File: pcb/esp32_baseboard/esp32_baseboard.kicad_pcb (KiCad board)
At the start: 2 copper layers, 180 x 120 mm, 84 parts, among them J1 24V_IN, J14 BUP_U, J15 FIBER, U1 STM32G030, U2 MP1584EN, U3 TMC2209, U4 TMC2209, U44 PC817, U45 PC817, U46 PC817, U47 PC817, U5 CH340C, U6 AMS1117-3.3, Y1 12MHz

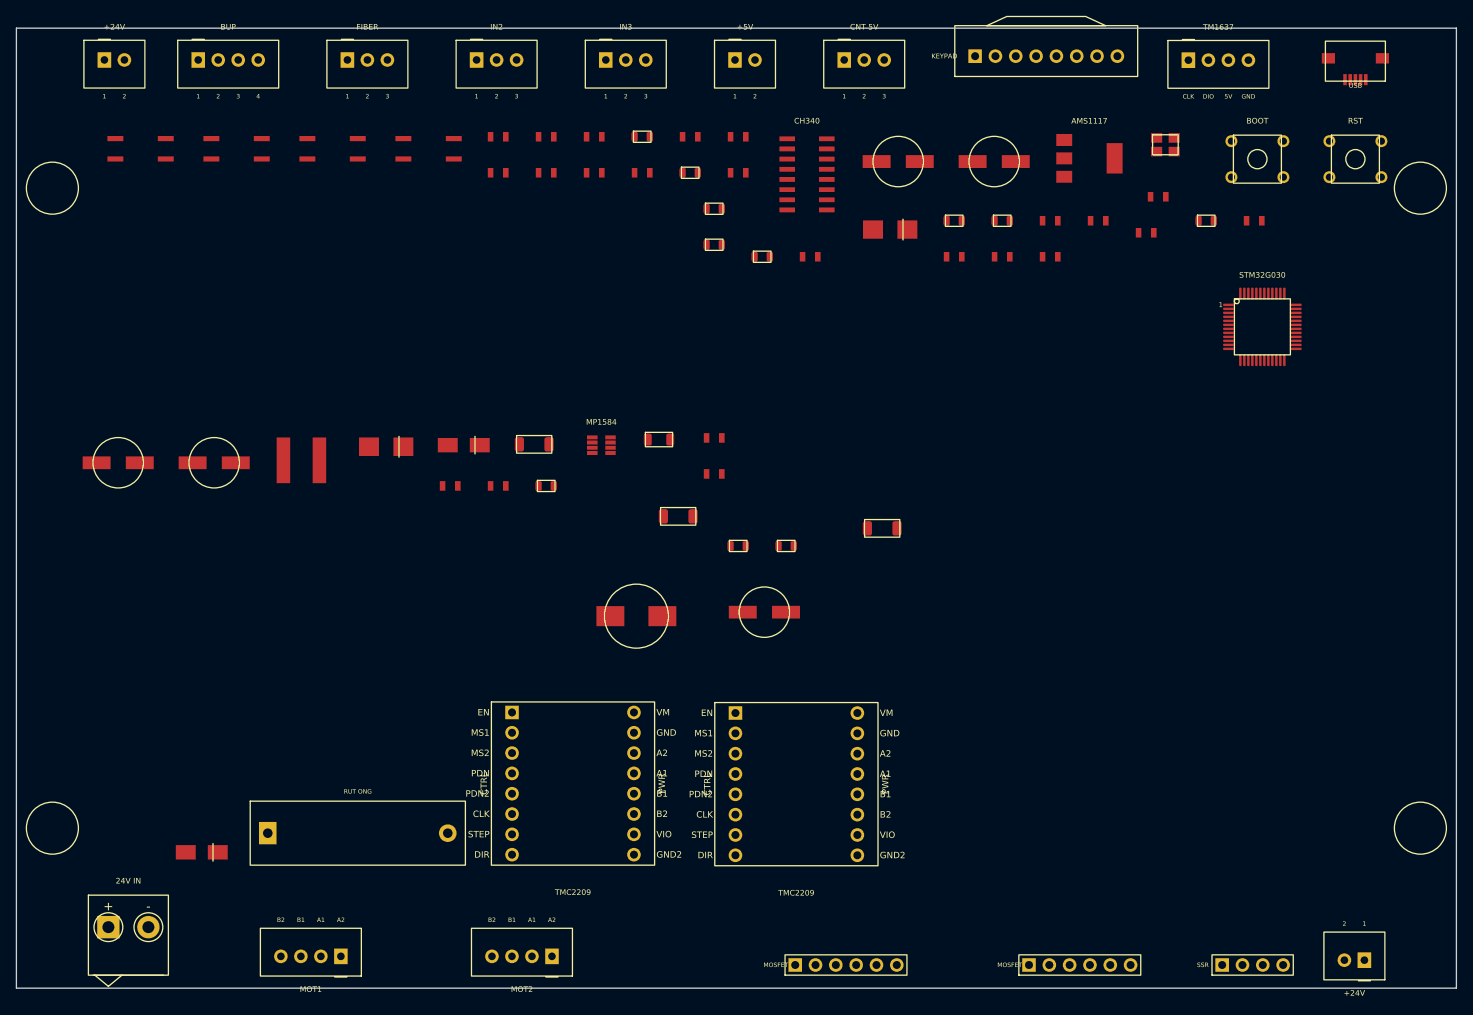
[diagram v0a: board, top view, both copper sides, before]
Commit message: thêm review JLCPCB và cập nhật BOM, bỏ tracking JRE/out.
Co-authored-by: Cursor <cursoragent@cursor.com>
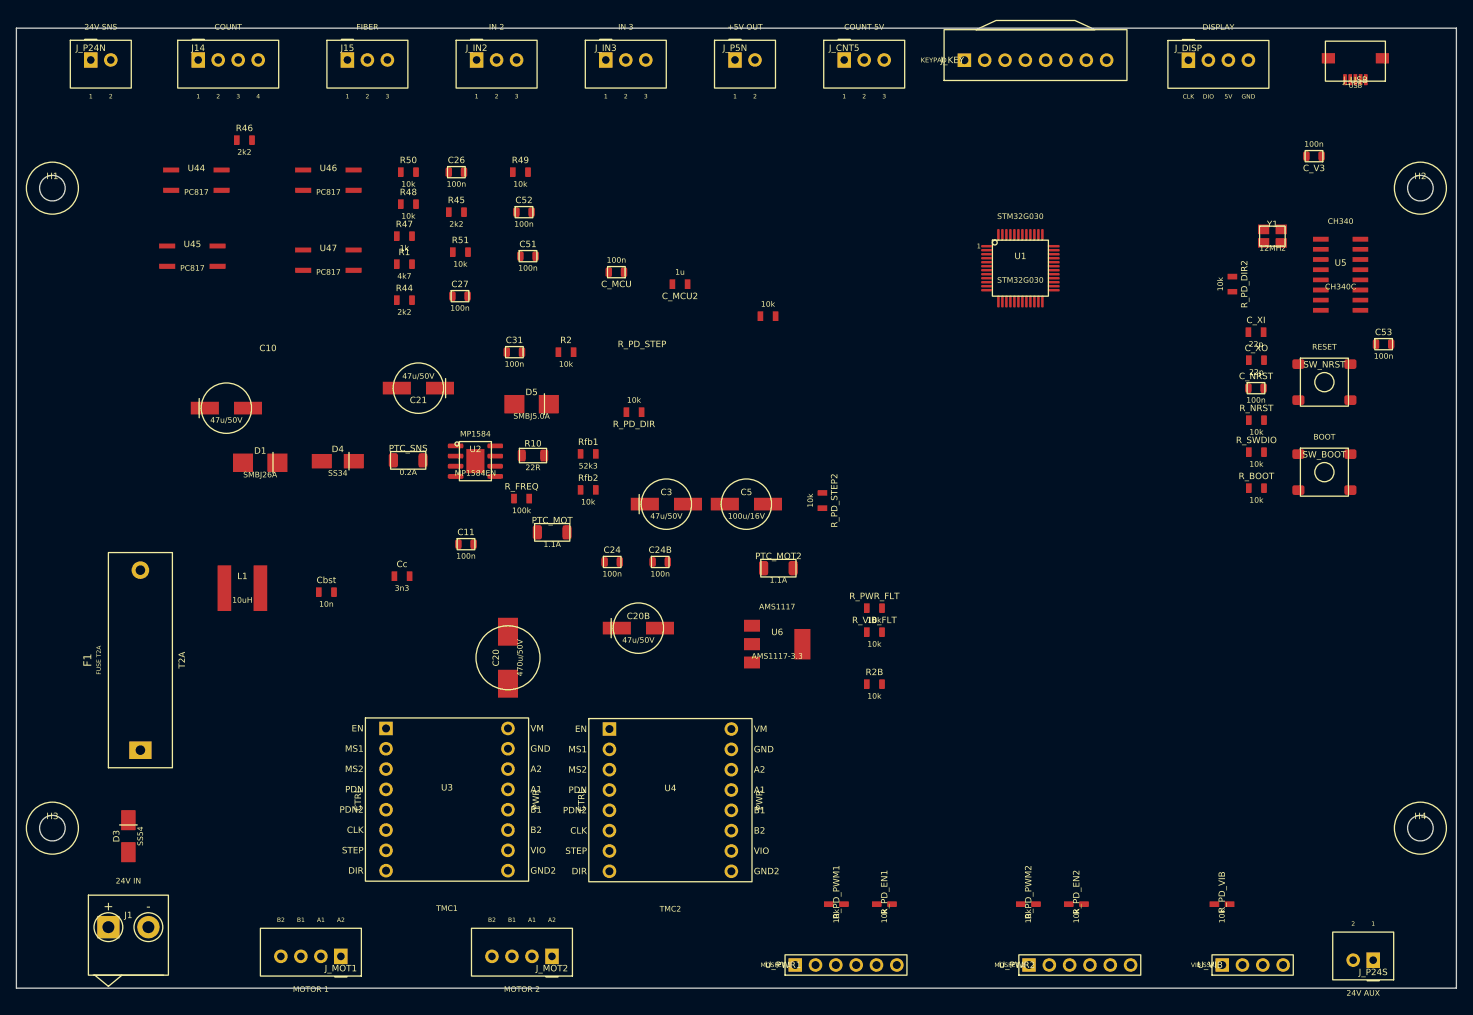
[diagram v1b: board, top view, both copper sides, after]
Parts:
- removed the C20B at (143.5, 123.0)
- added C20B: 47u/50V, ESP32_Carrier:CP_SMD_D6.3x8, F.Cu at (127.8, 125.0)
- added C_V3: 100n, ESP32_Carrier:C_0805_100n, F.Cu at (212.2, 66.0)
- added R_FREQ: 100k, ESP32_Carrier:R_0805_100k, F.Cu at (113.2, 108.8)
- added R_PD_DIR: 10k, ESP32_Carrier:R_0805_10k, F.Cu at (127.2, 98.0)
- added R_PD_DIR2: 10k, ESP32_Carrier:R_0805_10k, F.Cu at (202.0, 82.0)
- added R_PD_EN1: 10k, ESP32_Carrier:R_0805_10k, F.Cu at (158.5, 159.5)
- added R_PD_EN2: 10k, ESP32_Carrier:R_0805_10k, F.Cu at (182.5, 159.5)
- added R_PD_PWM1: 10k, ESP32_Carrier:R_0805_10k, F.Cu at (152.5, 159.5)
- added R_PD_PWM2: 10k, ESP32_Carrier:R_0805_10k, F.Cu at (176.5, 159.5)
- added R_PD_STEP: 10k, ESP32_Carrier:R_0805_10k, F.Cu at (143.9, 86.0)
- added R_PD_STEP2: 10k, ESP32_Carrier:R_0805_10k, F.Cu at (150.8, 109.0)
- added R_PD_VIB: 10k, ESP32_Carrier:R_0805_10k, F.Cu at (200.7, 159.5)
- C10: footprint ESP32_Carrier:CP_SMD_D6.3x5.8 -> ESP32_Carrier:CP_SMD_D6.3x8
- C21: value 220u/50V -> 47u/50V; footprint ESP32_Carrier:CP_SMD_D6.3x5.8 -> ESP32_Carrier:CP_SMD_D6.3x8
- C3: value 47u/10V -> 47u/50V; footprint ESP32_Carrier:CP_SMD_D6.3x5.8 -> ESP32_Carrier:CP_SMD_D6.3x8
- J1: value 24V_IN -> 24V IN
- J14: value BUP_U -> COUNT
- J_CNT5: value CNT5V -> COUNT 5V
- J_DISP: value TM1637 -> DISPLAY
- J_IN2: value IN2 -> IN 2
- J_IN3: value IN3 -> IN 3
- J_MOT1: value MOT1 -> MOTOR 1
- J_MOT2: value MOT2 -> MOTOR 2
- J_P24N: value P24_N -> 24V SNS
- J_P24S: value P24_S -> 24V AUX
- J_P5N: value P5_N -> +5V OUT
- SW_BOOT: value BOOT0 -> BOOT; footprint ESP32_Carrier:SW_Push_6mm -> ESP32_Carrier:SW_Push_6mm_SMD
- SW_NRST: value NRST -> RESET; footprint ESP32_Carrier:SW_Push_6mm -> ESP32_Carrier:SW_Push_6mm_SMD
- U2: footprint ESP32_Carrier:MP1584EN_SOT23-8 -> ESP32_Carrier:MP1584EN_SOIC-8-EP
- U3: value TMC2209 -> TMC1
- U4: value TMC2209 -> TMC2
- U_PWR1: value MOSFET -> MOSFET 1
- U_PWR2: value MOSFET -> MOSFET 2
- U_VIB: value SSR -> VIB SSR
- moved U6 72.2 mm to (145.1, 127.0)
- moved U5 67.9 mm to (215.5, 80.8)
- moved C_XI 67.7 mm to (204.9, 88.0)
- moved C3 59.3 mm to (131.2, 109.5)
- moved C53 55.8 mm to (220.9, 89.5)
- moved R2B 54.3 mm to (157.2, 132.0)
- moved R_VIB_FLT 51.8 mm to (157.2, 125.5)
- moved D5 49.9 mm to (114.4, 97.0)
- moved C_MCU 48.7 mm to (125.0, 80.5), turned to 180 degrees
- moved C_MCU2 46.9 mm to (132.9, 82.0), turned to 180 degrees
- moved C5 46.8 mm to (141.2, 109.5)
- moved R_PWR_FLT 46.7 mm to (157.2, 122.5)
- moved SW_BOOT 40.0 mm to (213.5, 105.5)
- moved F1 34.7 mm to (65.5, 129.0), turned to 90 degrees
- moved R_BOOT 33.4 mm to (205.0, 107.5)
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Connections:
- U2 pad 2: +24V -> (no net)
- U2 pad 6: +24V -> /BUCK_FREQ
- U2 pad 7: unconnected-(U2-P7-Pad7) -> +24V
- U5 pad 4: +3V3 -> /CH340_V3
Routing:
- added copper zone on In2.Cu, net +24V
- added copper zone on In2.Cu, net +3V3
- added copper zone on In2.Cu, net +5V
- added copper zone on In1.Cu, net GND
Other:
- copper layers 2 -> 4
